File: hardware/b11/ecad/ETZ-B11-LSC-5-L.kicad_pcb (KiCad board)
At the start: 2 copper layers, 112.3 x 85.8 mm, 0 parts

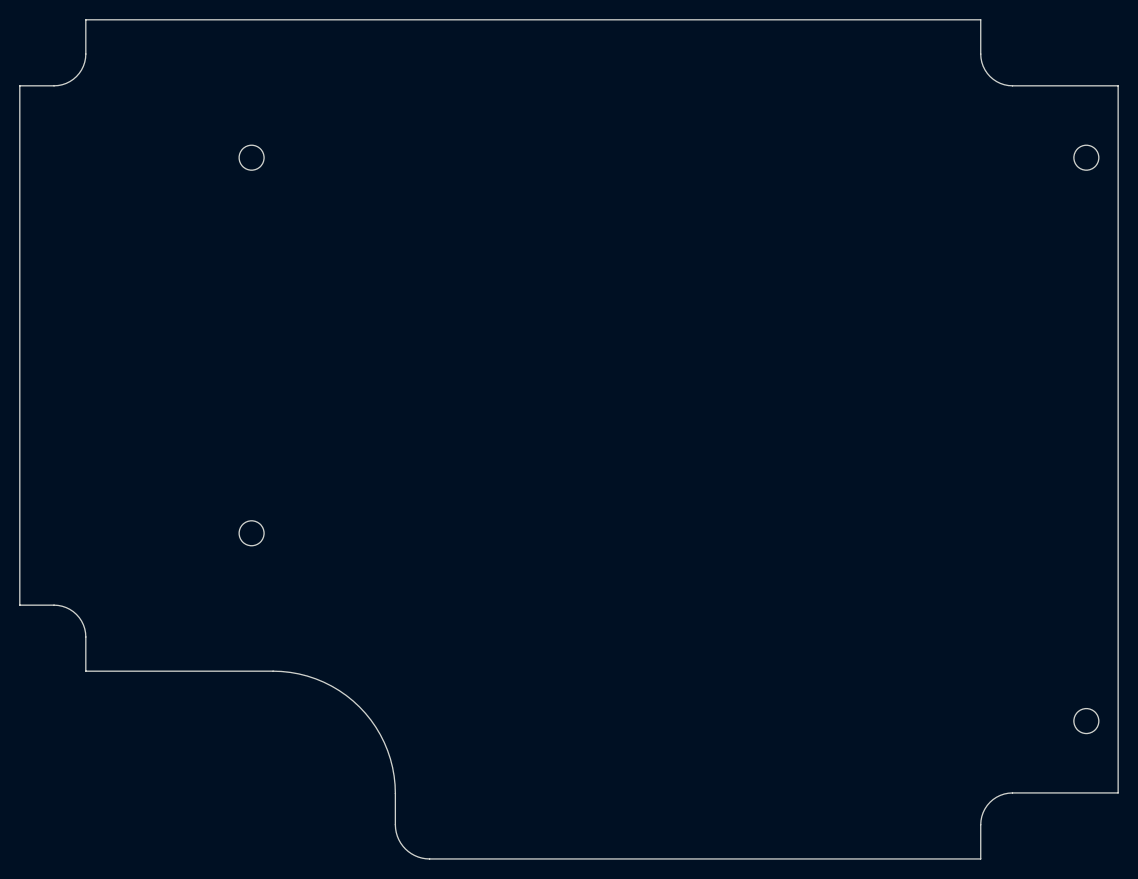
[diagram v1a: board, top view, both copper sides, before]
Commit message: feat(hardware/b11): place hotswap sockets on all carrier boards, south-facing
- Place Kailh MX hotswap sockets (MX-Hotswap-1U) on 4 normal-profile carrier
  boards at 19.2mm pitch, flipped to B.Cu, 180° south-facing orientation
- Place Kailh Choc v1 hotswap sockets (PG1350) on 4 low-profile carrier boards
  at 19.2mm pitch, 180° south-facing orientation
- Add 3D model (Kailh-Choc-Socket-CPG135001S30.step) to PG1350 footprint with
  correct offset/rotation for B.Cu-pad, F.Cu-module placement
- Strip F.SilkS, F.Fab, F.CrtYd top-layer graphics from LP carrier PG1350 footprints
- Rename place-b11-switches.py → place-b11-switches-np.py for symmetry with new lp script
- Add place-b11-switches-lp.py for Choc v1 placement automation

Co-Authored-By: Claude Sonnet 4.6 <noreply@anthropic.com>
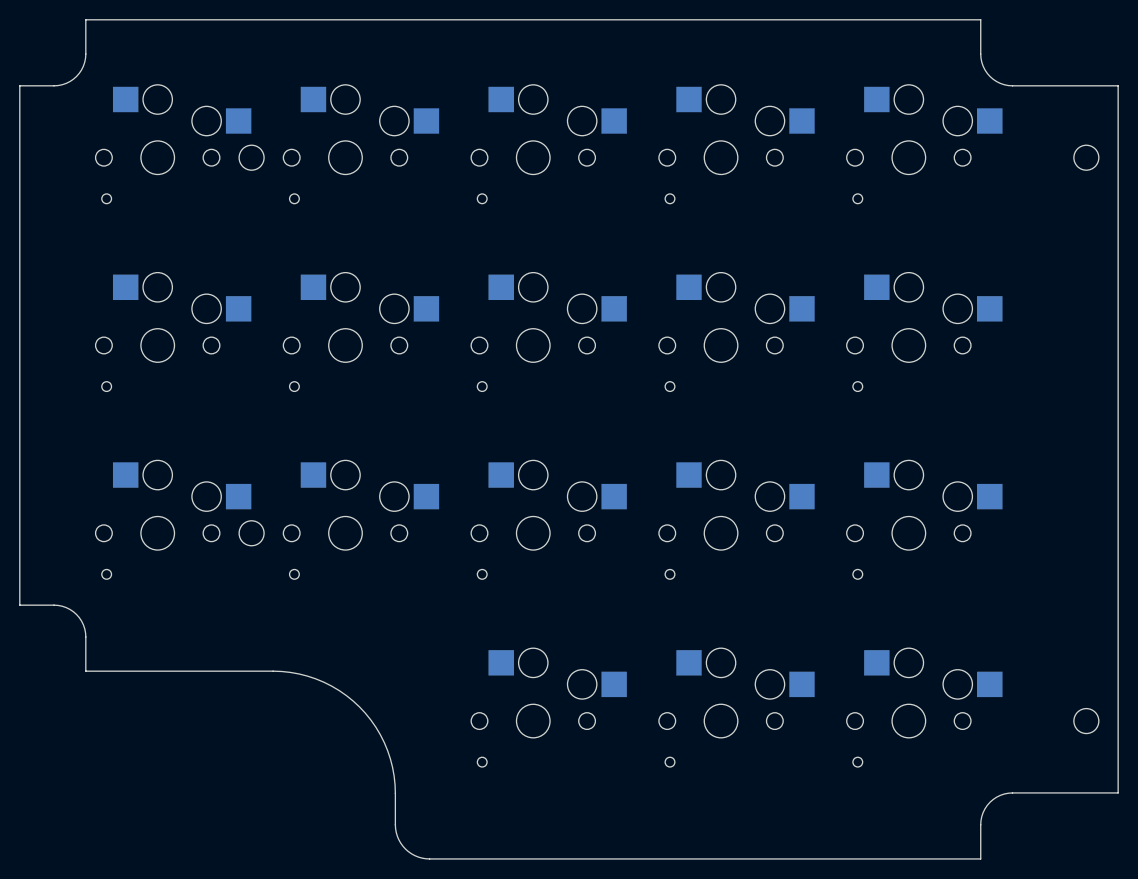
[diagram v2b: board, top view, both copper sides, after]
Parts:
- added SW1: Kailh_socket_PG1350, Kailh_socket_PG1350, F.Cu at (106.4, 73.3)
- added SW10: Kailh_socket_PG1350, Kailh_socket_PG1350, F.Cu at (183.2, 92.5)
- added SW11: Kailh_socket_PG1350, Kailh_socket_PG1350, F.Cu at (106.4, 111.7)
- added SW12: Kailh_socket_PG1350, Kailh_socket_PG1350, F.Cu at (125.6, 111.7)
- added SW13: Kailh_socket_PG1350, Kailh_socket_PG1350, F.Cu at (144.8, 111.7)
- added SW14: Kailh_socket_PG1350, Kailh_socket_PG1350, F.Cu at (164.0, 111.7)
- added SW15: Kailh_socket_PG1350, Kailh_socket_PG1350, F.Cu at (183.2, 111.7)
- added SW16: Kailh_socket_PG1350, Kailh_socket_PG1350, F.Cu at (144.8, 130.9)
- added SW17: Kailh_socket_PG1350, Kailh_socket_PG1350, F.Cu at (164.0, 130.9)
- added SW18: Kailh_socket_PG1350, Kailh_socket_PG1350, F.Cu at (183.2, 130.9)
- added SW2: Kailh_socket_PG1350, Kailh_socket_PG1350, F.Cu at (125.6, 73.3)
- added SW3: Kailh_socket_PG1350, Kailh_socket_PG1350, F.Cu at (144.8, 73.3)
- added SW4: Kailh_socket_PG1350, Kailh_socket_PG1350, F.Cu at (164.0, 73.3)
- added SW5: Kailh_socket_PG1350, Kailh_socket_PG1350, F.Cu at (183.2, 73.3)
- added SW6: Kailh_socket_PG1350, Kailh_socket_PG1350, F.Cu at (106.4, 92.5)
- added SW7: Kailh_socket_PG1350, Kailh_socket_PG1350, F.Cu at (125.6, 92.5)
- added SW8: Kailh_socket_PG1350, Kailh_socket_PG1350, F.Cu at (144.8, 92.5)
- added SW9: Kailh_socket_PG1350, Kailh_socket_PG1350, F.Cu at (164.0, 92.5)

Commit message: feat(hardware/b11): add SMD 6028 back-mount LED footprint and place on all carrier PCBs
- Add LED_SMD_6028_BackMount footprint with router-safe rounded-rectangle
  slot cutout (3.3 × 3.9 mm, 0.5 mm corners, 1 mm bit), roundrect pads
  (1.4 × 2.8 mm, 25% ratio), silkscreen polarity markers clear of pads
- Add LED_SMD_6028.step 3D model from 3D Content Central
- Add place-b11-leds.py: places 18–22 LEDs per carrier PCB aligned to
  the switch grid, 5.9 mm south of each switch center
- Place LEDs on all 8 carrier PCBs (LSC/RSC × 5/6-col × N/L)

Co-Authored-By: Claude Sonnet 4.6 <noreply@anthropic.com>
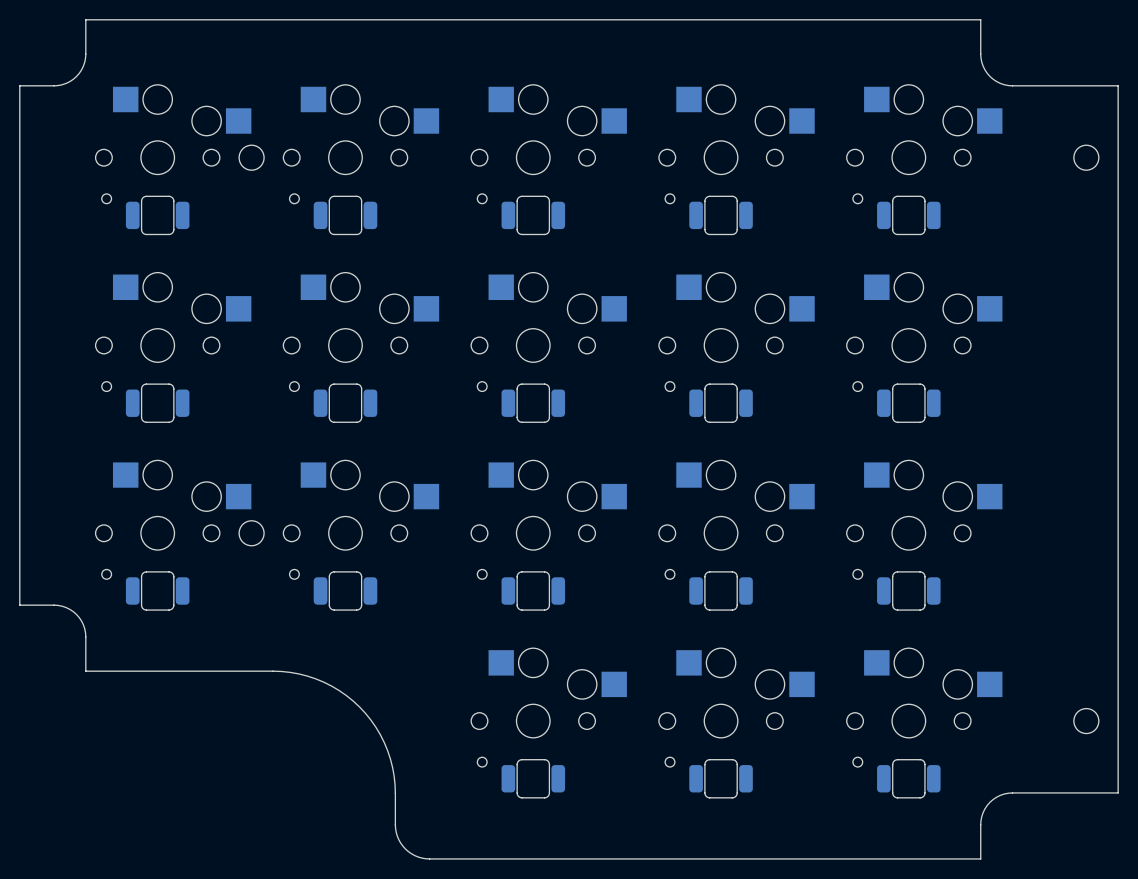
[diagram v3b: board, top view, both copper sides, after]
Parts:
- added LED1: LED_SMD_6028_BackMount, LED_SMD_6028_BackMount, B.Cu at (106.4, 79.2)
- added LED10: LED_SMD_6028_BackMount, LED_SMD_6028_BackMount, B.Cu at (183.2, 98.4)
- added LED11: LED_SMD_6028_BackMount, LED_SMD_6028_BackMount, B.Cu at (106.4, 117.6)
- added LED12: LED_SMD_6028_BackMount, LED_SMD_6028_BackMount, B.Cu at (125.6, 117.6)
- added LED13: LED_SMD_6028_BackMount, LED_SMD_6028_BackMount, B.Cu at (144.8, 117.6)
- added LED14: LED_SMD_6028_BackMount, LED_SMD_6028_BackMount, B.Cu at (164.0, 117.6)
- added LED15: LED_SMD_6028_BackMount, LED_SMD_6028_BackMount, B.Cu at (183.2, 117.6)
- added LED16: LED_SMD_6028_BackMount, LED_SMD_6028_BackMount, B.Cu at (144.8, 136.8)
- added LED17: LED_SMD_6028_BackMount, LED_SMD_6028_BackMount, B.Cu at (164.0, 136.8)
- added LED18: LED_SMD_6028_BackMount, LED_SMD_6028_BackMount, B.Cu at (183.2, 136.8)
- added LED2: LED_SMD_6028_BackMount, LED_SMD_6028_BackMount, B.Cu at (125.6, 79.2)
- added LED3: LED_SMD_6028_BackMount, LED_SMD_6028_BackMount, B.Cu at (144.8, 79.2)
- added LED4: LED_SMD_6028_BackMount, LED_SMD_6028_BackMount, B.Cu at (164.0, 79.2)
- added LED5: LED_SMD_6028_BackMount, LED_SMD_6028_BackMount, B.Cu at (183.2, 79.2)
- added LED6: LED_SMD_6028_BackMount, LED_SMD_6028_BackMount, B.Cu at (106.4, 98.4)
- added LED7: LED_SMD_6028_BackMount, LED_SMD_6028_BackMount, B.Cu at (125.6, 98.4)
- added LED8: LED_SMD_6028_BackMount, LED_SMD_6028_BackMount, B.Cu at (144.8, 98.4)
- added LED9: LED_SMD_6028_BackMount, LED_SMD_6028_BackMount, B.Cu at (164.0, 98.4)

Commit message: fix(hardware/b11): fix switch socket placement, 3D models, and submodule pins
- Pin MX_V2 submodule to ab59b57 (before upstream "topside pads" change that
  moved SMD pads to F.Cu — old commit has correct B.Cu pads natively)
- Fix SWIG type-registry corruption in both switch placement scripts by
  pre-loading all footprint instances and caching pad refs before LoadBoard()
- Fix LP script: add make_patched_lib to rewrite Choc socket 3D model path
  to absolute path and convert old (at ...) inch offset to (offset ...) mm
  format — KiCad 9 was multiplying the old format by 25.4, placing model
  127mm off-center
- Regenerate all 8 carrier PCBs with updated board outlines (LSC-6 mounting
  hole positions) and correctly placed switches + LEDs

Co-Authored-By: Claude Sonnet 4.6 <noreply@anthropic.com>
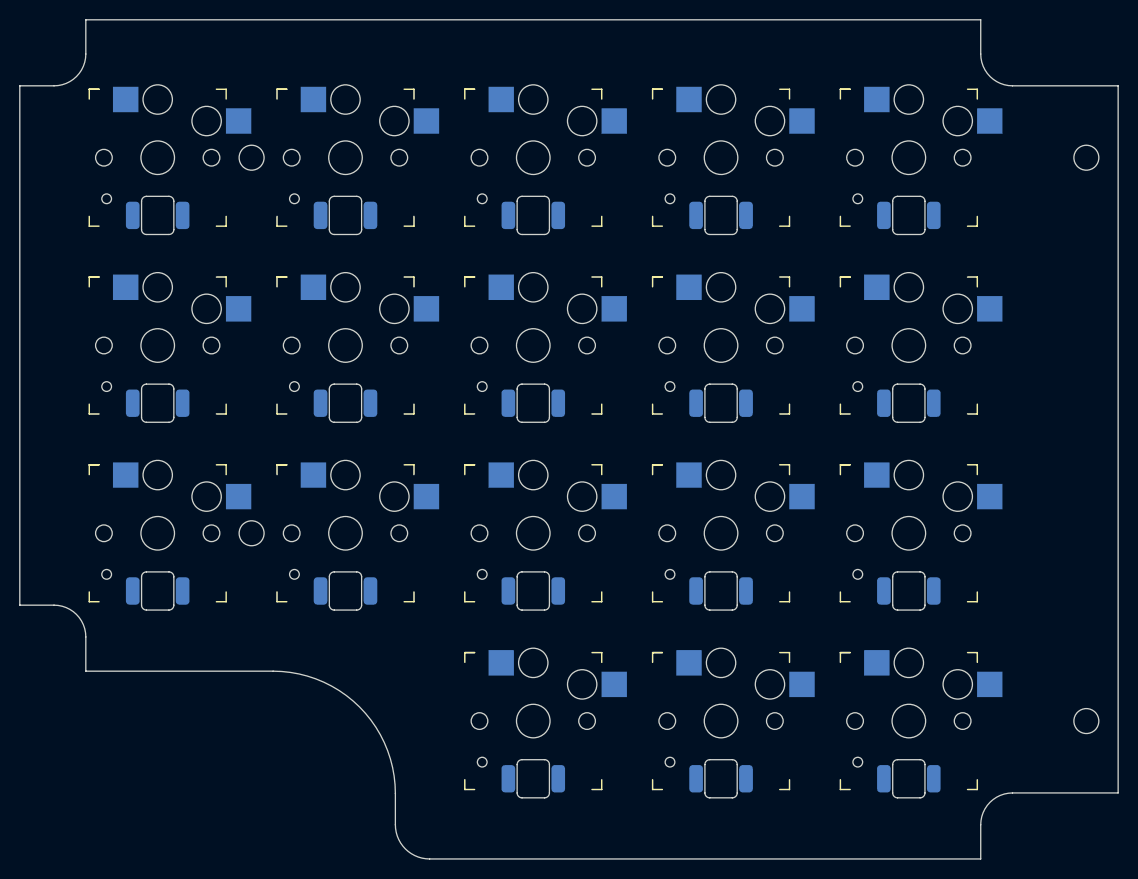
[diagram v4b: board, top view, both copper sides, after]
